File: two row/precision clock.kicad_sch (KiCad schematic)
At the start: 47 parts, among them P1 USB_C_Plug_USB2.0, P2 USB_C_Plug_USB2.0, Q1 MMBT3906, Q2 MMBT3906

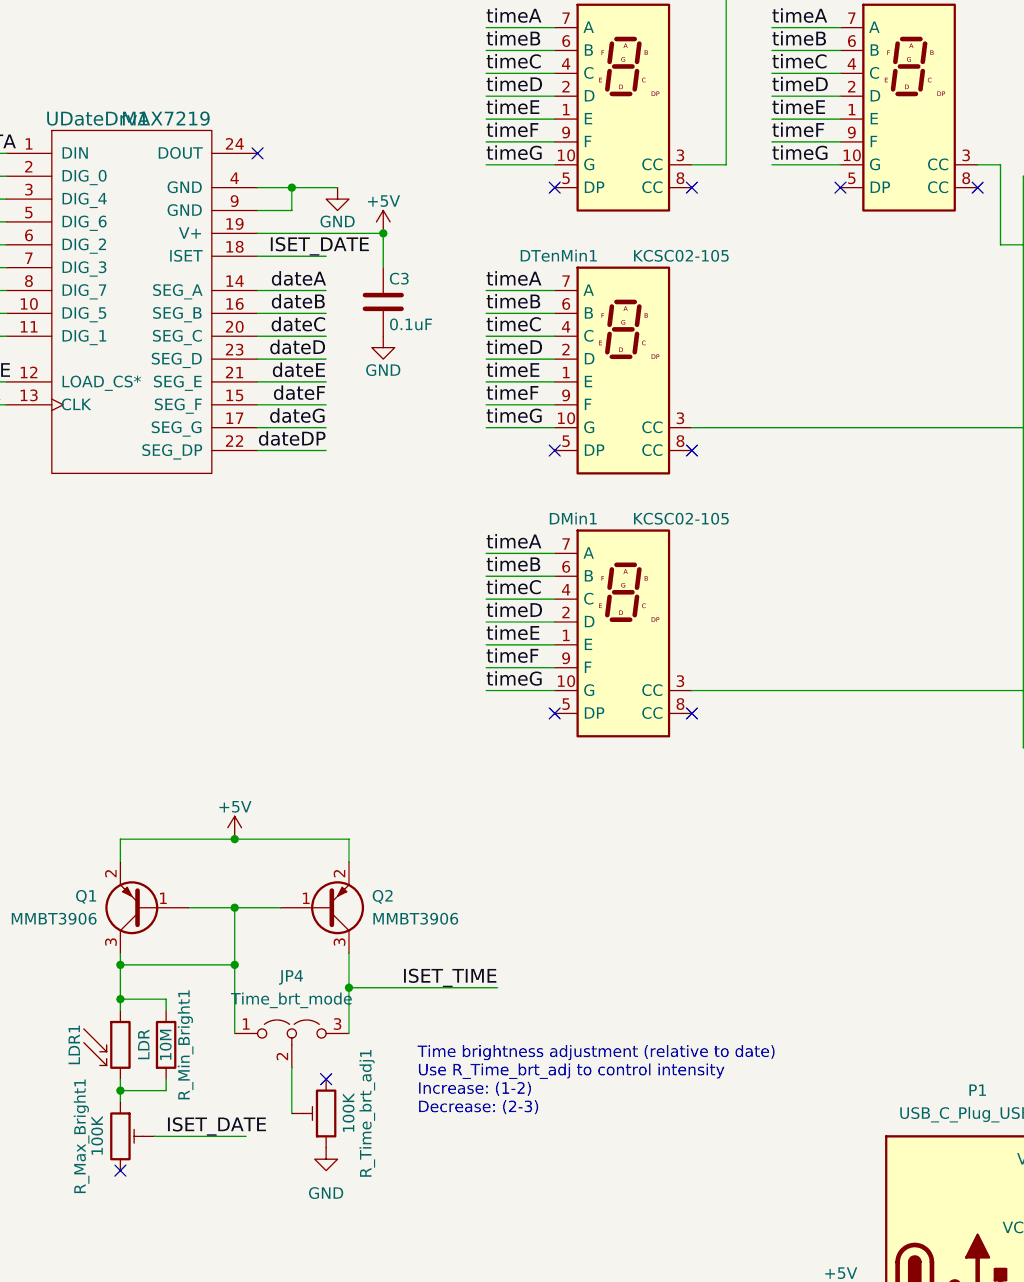
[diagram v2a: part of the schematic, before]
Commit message: Add wire to seconds decimal point
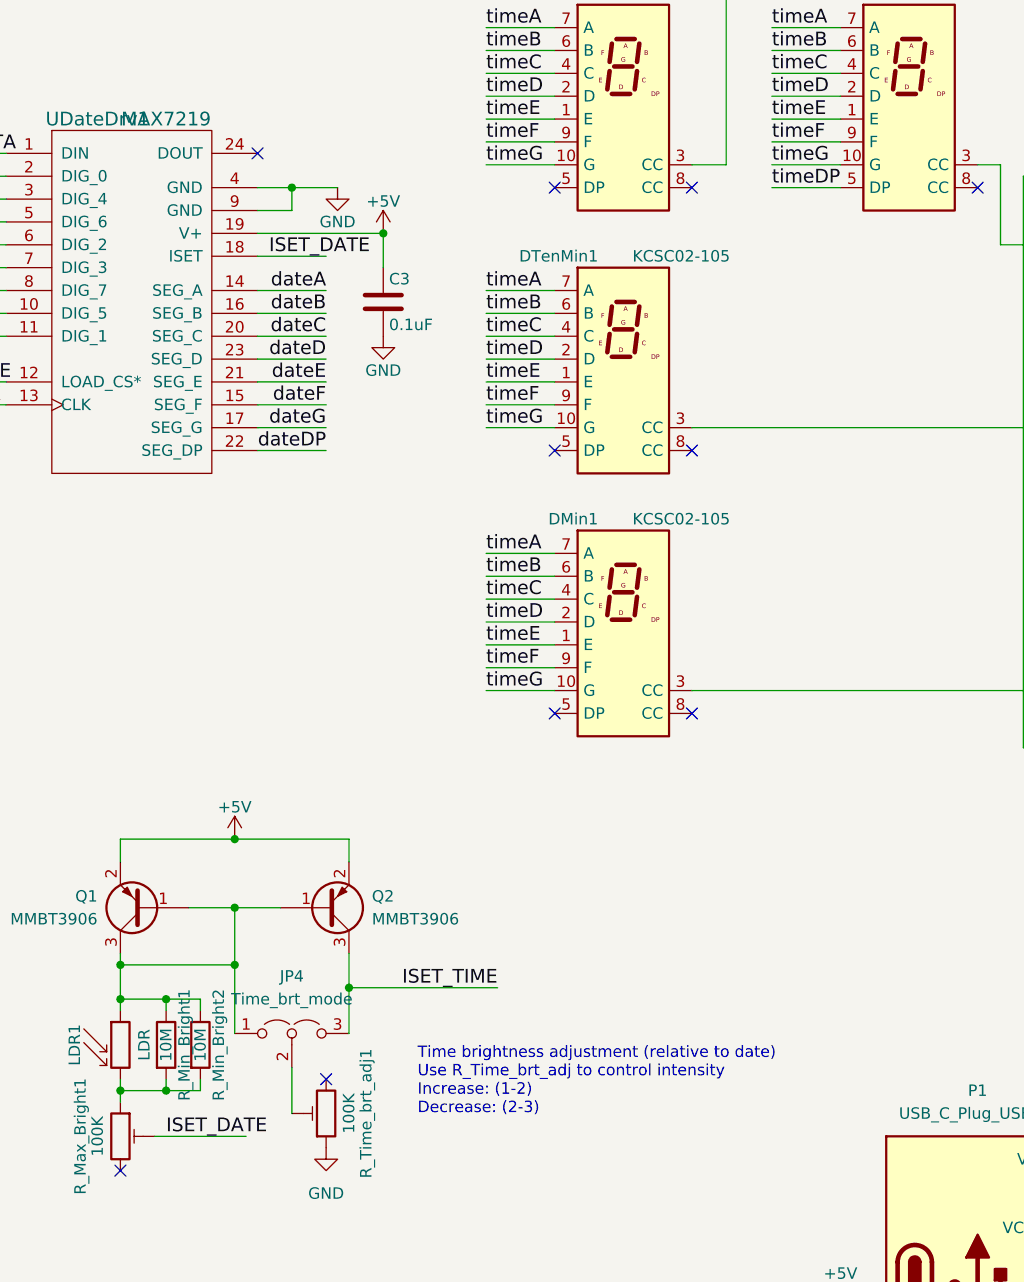
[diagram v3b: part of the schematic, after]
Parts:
- added R_Min_Bright2: 10M, Resistor_SMD:R_1206_3216Metric, symbol precision-clock-rescue:R
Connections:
- net timeDP: now also DSec1.5 (DP)
- net at JP4.1 (A), LDR1.1, Q1.1 (B)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: now also R_Min_Bright2.1
- net at LDR1.2, R_Max_Bright1.1, R_Min_Bright1.2: now also R_Min_Bright2.2
- no-connect marks 65 -> 64
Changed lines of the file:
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@@
 	)
 	(junction
+		(at 127 160.02)
+		(diameter 0)
+		(color 0 0 0 0)
+	)
+	(junction
 		(at 22.86 224.79)
 		(diameter 0)
@@
 	)
 	(junction
+		(at 127 170.18)
+		(diameter 0)
+		(color 0 0 0 0)
+	)
+	(junction
 		(at 50.8 133.35)
 		(diameter 0)
@@
 	)
 	(no_connect
-		(at 201.93 69.85)
-	)
-	(no_connect
 		(at 121.92 179.07)
 	)
@@
 	(wire
 		(pts
+			(xy 127 160.02) (xy 130.81 160.02)
+		)
+		(stroke
+			(width 0)
+			(type default)
+		)
+	)
+	(wire
+		(pts
 			(xy 96.52 81.28) (xy 96.52 15.24)
 		)
@@
 	(wire
 		(pts
+			(xy 201.93 69.85) (xy 194.31 69.85)
+		)
+		(stroke
+			(width 0)
+			(type default)
+		)
+	)
+	(wire
+		(pts
 			(xy 129.54 149.86) (xy 134.62 149.86)
 		)
@@
 	(wire
 		(pts
+			(xy 130.81 170.18) (xy 127 170.18)
+		)
+		(stroke
+			(width 0)
+			(type default)
+		)
+	)
+	(wire
+		(pts
 			(xy 274.32 121.92) (xy 274.32 124.46)
 		)
@@
 	(wire
 		(pts
+			(xy 130.81 168.91) (xy 130.81 170.18)
+		)
+		(stroke
+			(width 0)
+			(type default)
+		)
+	)
+	(wire
+		(pts
 			(xy 109.22 68.58) (xy 83.82 68.58)
 		)
@@
 	(wire
 		(pts
+			(xy 130.81 161.29) (xy 130.81 160.02)
+		)
+		(stroke
+			(width 0)
+			(type default)
+		)
+	)
+	(wire
+		(pts
 			(xy 137.16 86.36) (xy 144.78 86.36)
 		)
@@
 		)
 	)
+	(label "timeDP"
+		(at 194.31 69.85 0)
+		(fields_autoplaced yes)
+		(effects
+			(font
+				(size 1.524 1.524)
+			)
+			(justify left bottom)
+		)
+	)
 	(label "dateB"
 		(at 24.13 113.03 0)
@@
 					(unit 1)
 				)
+			)
+		)
+	)
+	(symbol
+		(lib_id "precision-clock-rescue:R")
+		(at 130.81 165.1 0)
+		(unit 1)
+		(exclude_from_sim no)
+		(in_bom yes)
+		(on_board yes)
+		(dnp no)
+		(property "Reference" "R_Min_Bright2"
+			(at 132.842 165.1 90)
+			(effects
+				(font
+					(size 1.27 1.27)
+				)
+			)
+		)
+		(property "Value" "10M"
+			(at 130.81 165.1 90)
+			(effects
+				(font
+					(size 1.27 1.27)
+				)
+			)
+		)
+		(property "Footprint" "Resistor_SMD:R_1206_3216Metric"
+			(at 129.032 165.1 90)
+			(effects
+				(font
+					(size 1.27 1.27)
+				)
+				(hide yes)
+			)
+		)
+		(property "Datasheet" ""
+			(at 130.81 165.1 0)
+			(effects
+				(font
+					(size 1.27 1.27)
+				)
+				(hide yes)
+			)
+		)
+		(property "Description" ""
+			(at 130.81 165.1 0)
+			(effects
+				(font
+					(size 1.27 1.27)
+				)
+				(hide yes)
+			)
+		)
+		(pin "2"
+		)
+		(pin "1"
+		)
+		(instances
+			(project "precision clock"
+				(path "/a352d3ae-caca-4fe6-94e2-4912021cb238"
+					(reference "R_Min_Bright2")
+					(unit 1)
+				)

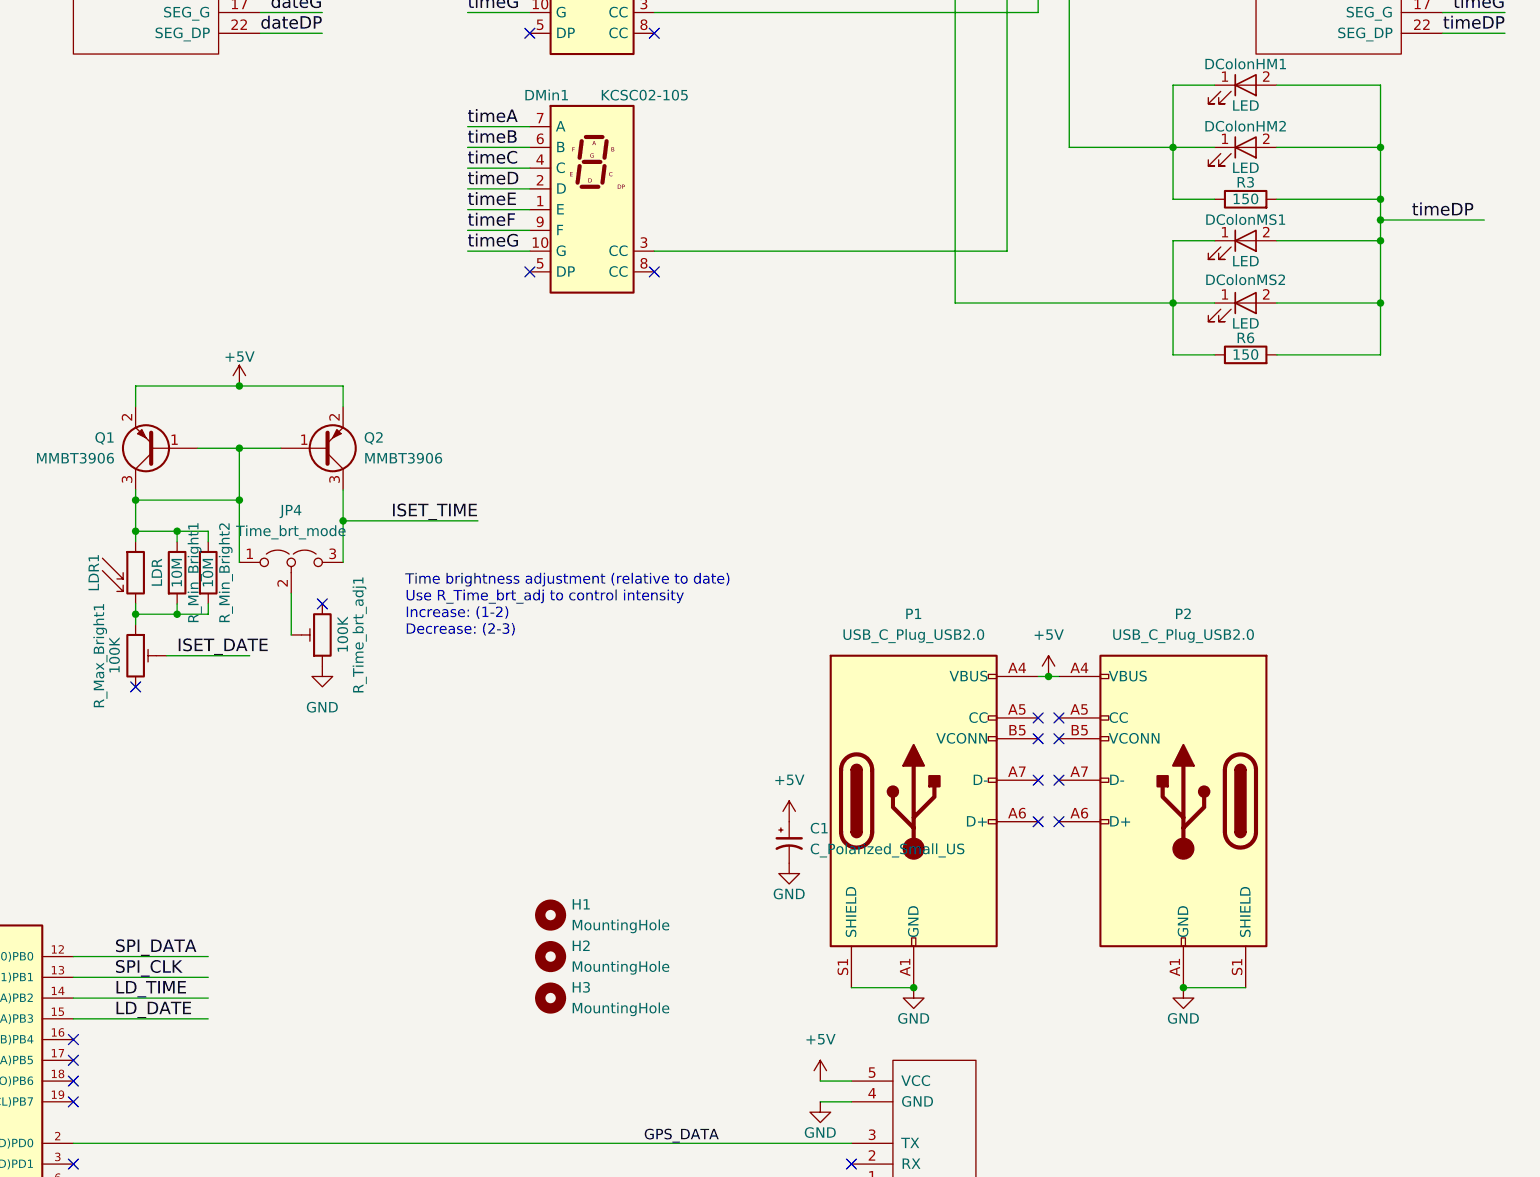
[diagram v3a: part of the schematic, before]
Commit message: Fixed USB-C pinout and CC resistors
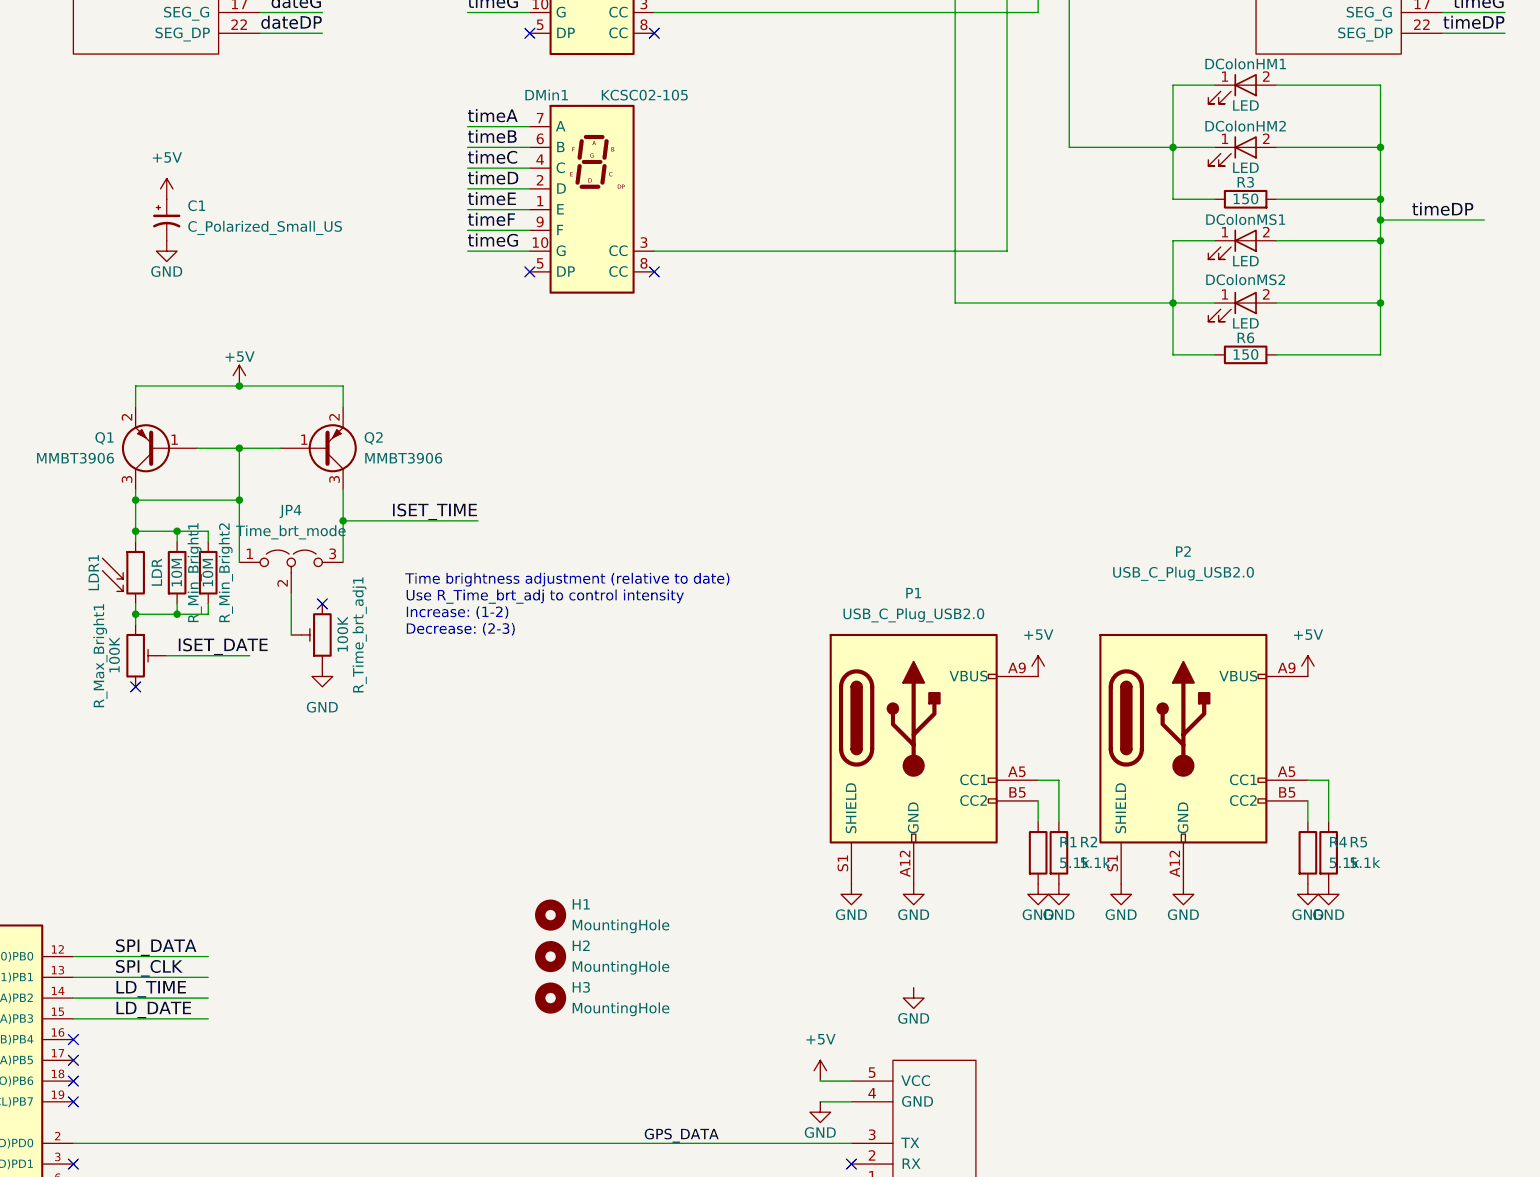
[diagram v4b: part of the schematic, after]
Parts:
- added R1, R2, R4, R5: 5.1k, Resistor_SMD:R_1206_3216Metric, symbol Device:R
- P1, P2: symbol Connector:USB_C_Plug_USB2.0 -> Connector:USB_C_Receptacle_PowerOnly_6P
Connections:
- net +5V: no longer P1.A4 (VBUS), P1.B4 (VBUS), P2.A4 (VBUS), P2.B4 (VBUS)
- net GND: now also R1.2, R2.2, R4.2, R5.2; no longer P1.A1 (GND), P1.B1 (GND), P2.A1 (GND), P2.B1 (GND)
- net at P2.A5 (CC1): now also R5.1
- net at P2.B5 (CC2): now also R4.1
- net at P1.A5 (CC1): now also R2.1
- net at P1.B5 (CC2): now also R1.1
- no-connect marks 64 -> 56
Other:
- moved on the sheet: C1
